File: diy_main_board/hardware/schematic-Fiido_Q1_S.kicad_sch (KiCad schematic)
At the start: 12 parts, among them J1 Connector_4, J2 Connector_2, U1 Step-down converter to 3.3V, U2 ESP32-S3-DevKitC

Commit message: Updated Fiido Q1S to reflect the changes for CAN communication with VESC
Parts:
- added R5, R7: 3.3K, symbol Device:R
- added R6, R8: 2.2K, symbol Device:R
- added U3: TJA1050_module, symbol TJA1050:TJA1050_module
- C1: value 100nF -> 1uF
- R1: value 82R -> 1K
- R2: value 82R -> 10K
- renumbered Connector_2 to Connector_1, Connector_1 to Connector_2
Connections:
- net +5V: now also U3.2 (VCC)
- net GND: now also R6.2, R8.2, U3.1 (GND)
- net at U2.4 (GPIO4/ADC1_CH3): now also R7.2, R8.1
- net at U2.5 (GPIO5/ADC1_CH4): now also R5.2, R6.1
- net VESC-UART_RX: no longer names the net of U2.19 (GPIO13/ADC2_CH2)
- net VESC-UART_RX: no longer J2.1 (Pin_1)
- net VESC-UART_TX: no longer names the net of U2.20 (GPIO14/ADC2_CH3)
- net VESC-UART_TX: no longer J2.2 (Pin_2)
- new net CAN_H: J2.1 (Pin_1), U3.5 (CANH)
- new net CAN_L: J2.2 (Pin_2), U3.6 (CANL)
- new net CAN_RX: R7.1, U3.4 (CAN_RX)
- new net CAN_TX: R5.1, U3.3 (CAN_TX)
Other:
- note added: "TJA1050 CANBUS module"
- moved on the sheet: C1, C2, Connector_1, Connector_2, R1, R2, R3, R4

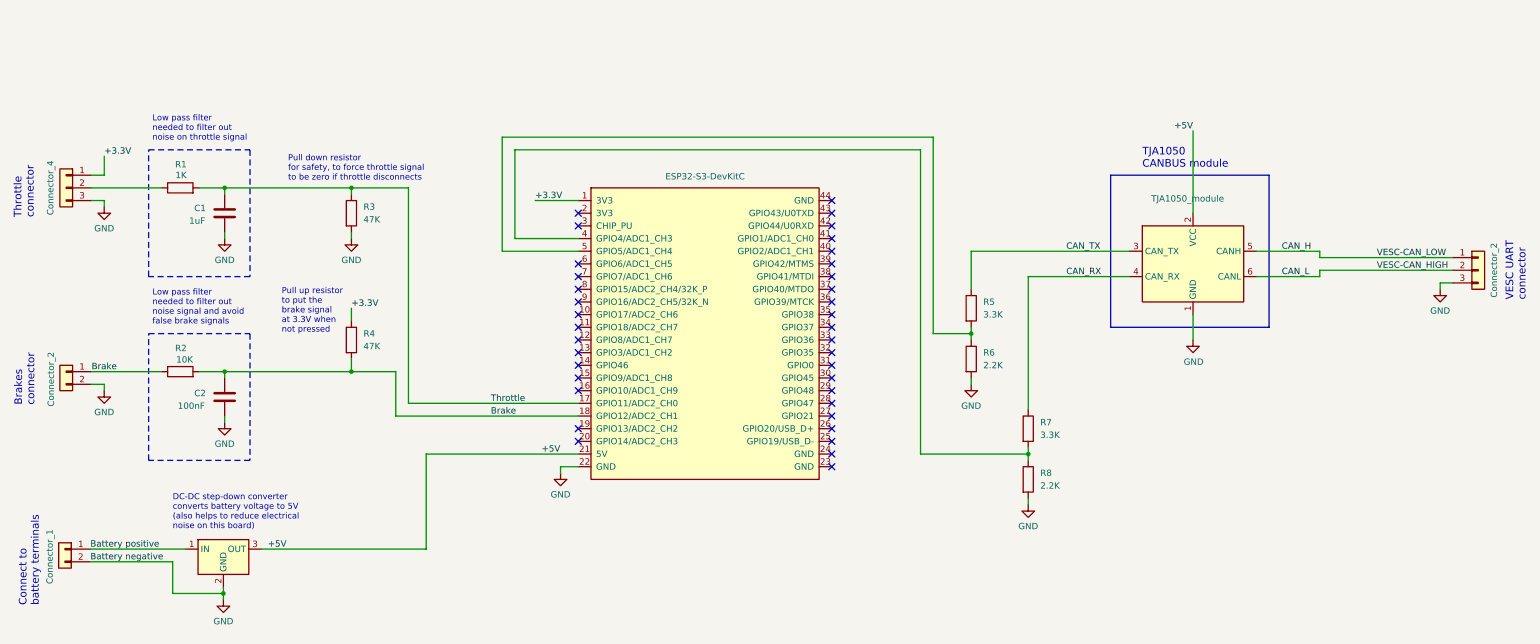
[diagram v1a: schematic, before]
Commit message: Small labeling change on schematic
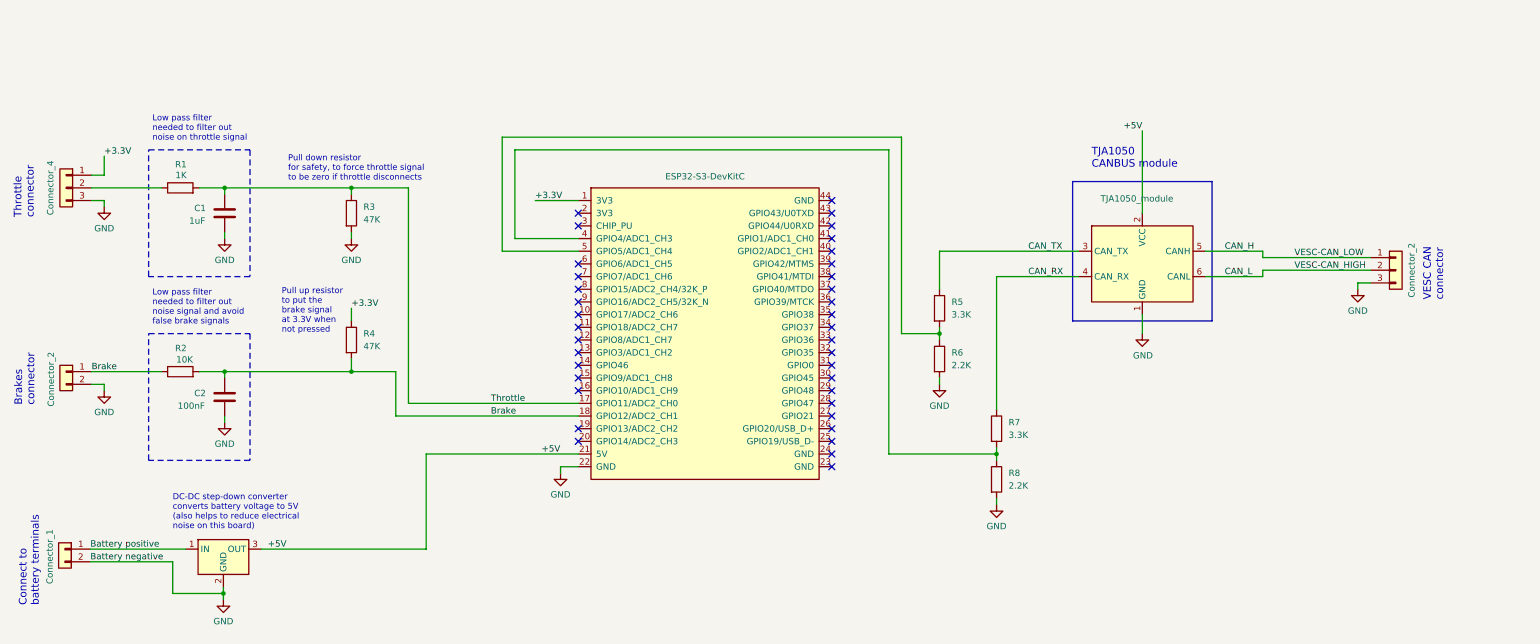
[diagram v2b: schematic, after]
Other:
- note added: "VESC CAN connector"
- note removed: "VESC UART connector"
- moved on the sheet: R5, R6, R7, R8

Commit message: Updated Fiido Q1S and Xiaomi_M365 main boards schematics
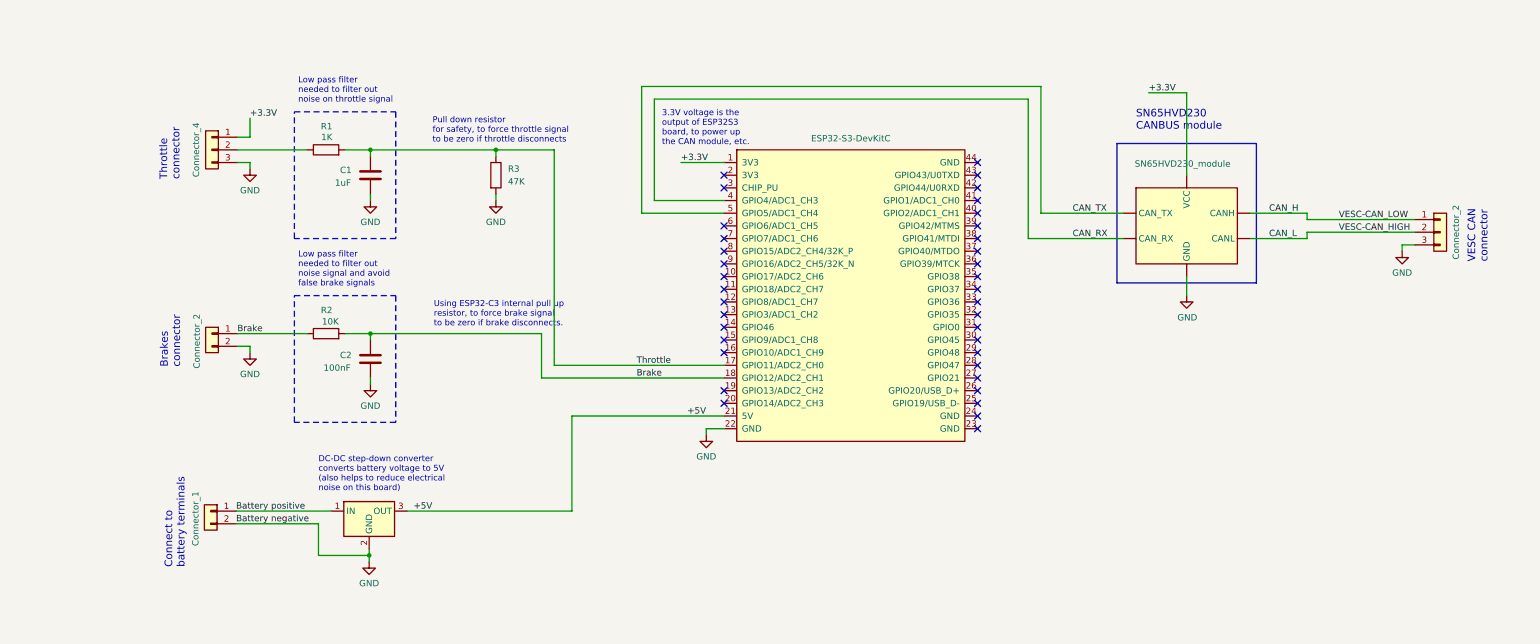
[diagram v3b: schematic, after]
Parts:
- removed R4: 47K, symbol Device:R
- removed R5, R7: 3.3K, symbol Device:R
- removed R6, R8: 2.2K, symbol Device:R
- U3: value TJA1050_module -> SN65HVD230_module
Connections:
- net +3.3V: now also U3. (VCC)
- net +5V: no longer U3.2 (VCC)
- net CAN_H: now also U3. (VCC); no longer U3.5 (CANH)
- net CAN_L: now also U3. (VCC); no longer U3.6 (CANL)
- net CAN_RX: now also U2.4 (GPIO4/ADC1_CH3), U3. (VCC); no longer U3.4 (CAN_RX)
- net CAN_TX: now also U2.5 (GPIO5/ADC1_CH4), U3. (VCC); no longer U3.3 (CAN_TX)
- net GND: now also U3. (VCC); no longer U3.1 (GND)
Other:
- note added: "3.3V voltage is the output of ESP32S3 board, to power up the CAN module, etc."
- note added: "SN65HVD230 CANBUS module"
- note added: "Using ESP32-C3 internal pull up resistor, to force brake signal to be zero if brake disconnects."
- note removed: "Pull up resistor to put the brake signal at 3.3V when not pressed"
- note removed: "TJA1050 CANBUS module"
- moved on the sheet: C1, C2, Connector_1, Connector_2, R1, R2

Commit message: Moved the main board from ESP32-S3 to ESP32-C3, because it is cheap and uses less power. I was also having an issue on ADC on S3 and on C3 it is ok
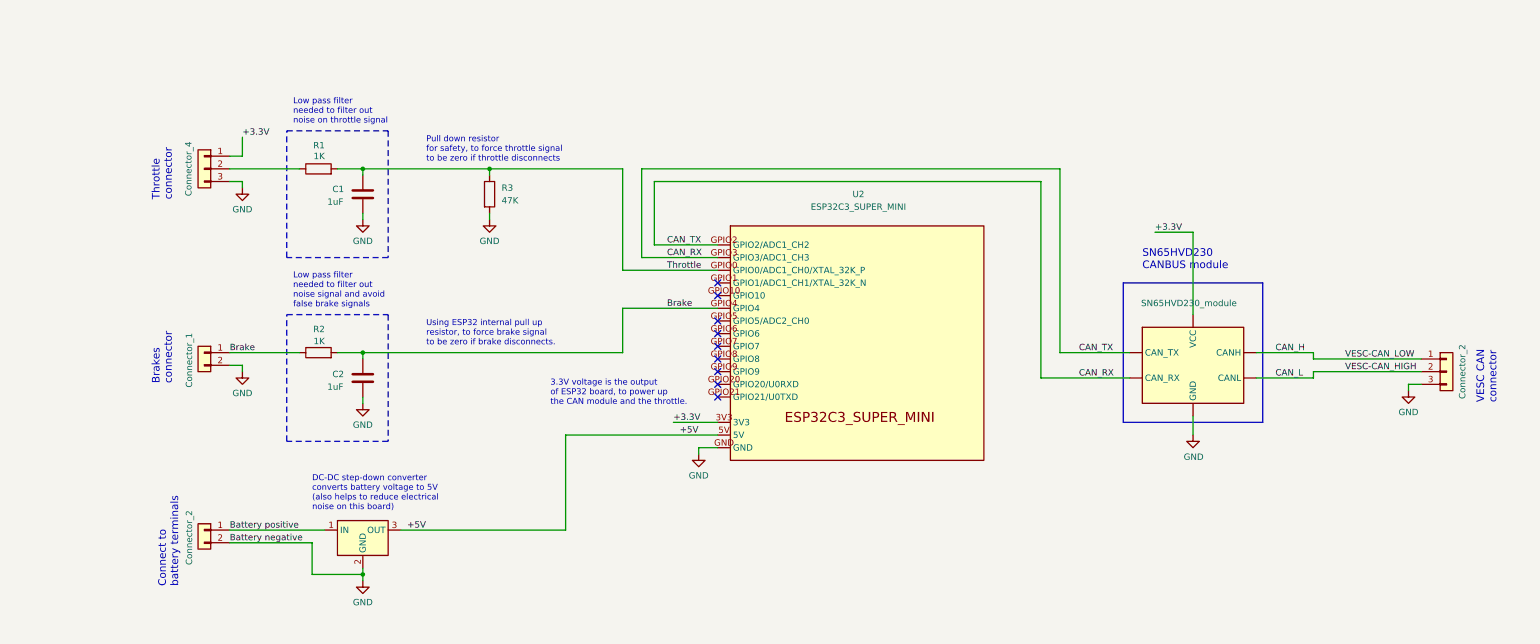
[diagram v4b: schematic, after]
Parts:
- removed U2: ESP32-S3-DevKitC, Espressif:ESP32-S3-DevKitC, symbol Espressif:ESP32-S3-DevKitC
- added U2: ESP32C3_SUPER_MINI, symbol Espressif:ESP32-C3-MINI-1
- C2: value 100nF -> 1uF
- R2: value 10K -> 1K
- renumbered Connector_2 to Connector_1, Connector_1 to Connector_2
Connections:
- net CAN_TX is gone; now on net GND: U3. (CANL)
- net +3.3V: now also U2.3V3
- net +5V: now also U2.5V
- net Brake: now also U2.GPIO4
- net CAN_RX: now also U2.GPIO2 (GPIO2/ADC1_CH2), U2.GPIO3 (GPIO3/ADC1_CH3)
- net GND: now also U2.GND
- net Throttle: now also U2.GPIO0 (GPIO0/ADC1_CH0/XTAL_32K_P)
- no-connect marks 37 -> 9
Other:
- note added: "3.3V voltage is the output of ESP32 board, to power up the CAN module and the throttle."
- note added: "Using ESP32 internal pull up resistor, to force brake signal to be zero if brake disconnects."
- note removed: "3.3V voltage is the output of ESP32S3 board, to power up the CAN module, etc."
- note removed: "Using ESP32-C3 internal pull up resistor, to force brake signal to be zero if brake disconnects."
- moved on the sheet: C1, C2, Connector_1, Connector_2, R1, R2, R3
